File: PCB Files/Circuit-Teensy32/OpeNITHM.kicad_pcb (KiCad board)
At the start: 2 copper layers, 100 x 45.3 mm, 26 parts, among them J1 Conn_01x14, J2 Conn_01x14, J3 Conn_02x07_Odd_Even, J7 Conn_02x12_Odd_Even, J8 Conn_02x12_Odd_Even, J9 Conn_01x05, U1 74HC4051, U2 74HC4051, U3 74HC4051, U4 74HC4051

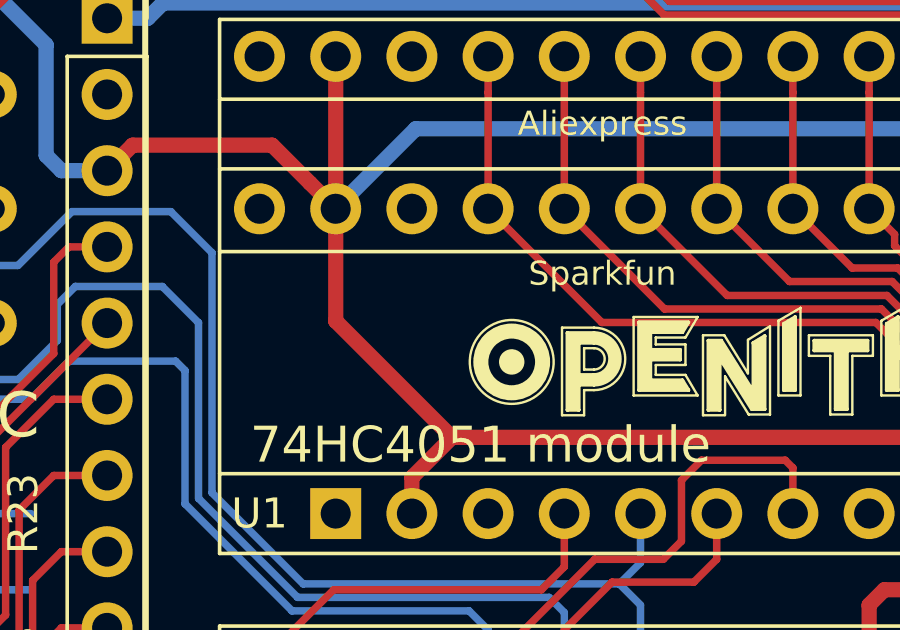
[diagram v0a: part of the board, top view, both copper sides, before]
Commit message: Fixed IR LED labeling on back silkscreen
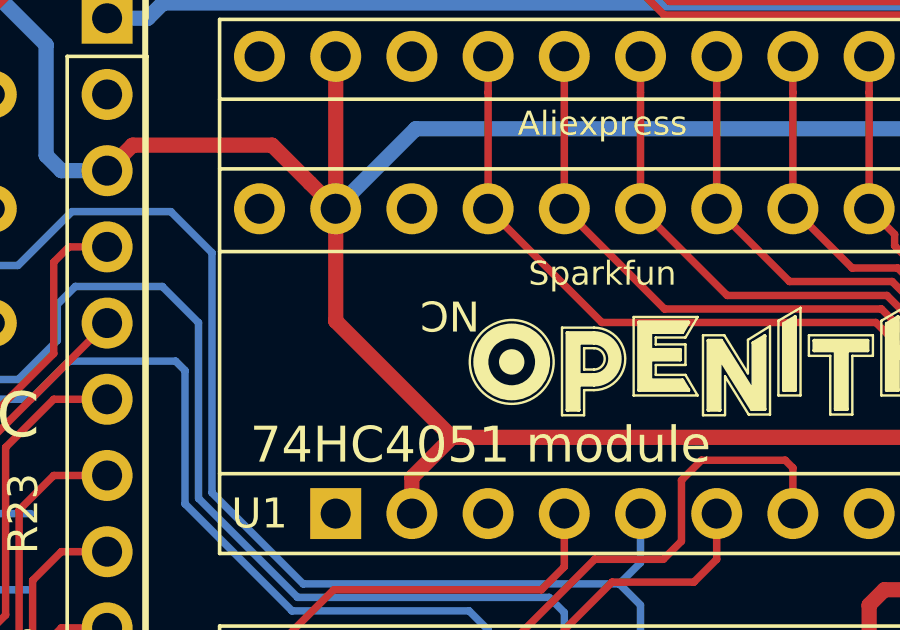
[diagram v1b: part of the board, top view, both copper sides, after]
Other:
- board text added: "VCC"
